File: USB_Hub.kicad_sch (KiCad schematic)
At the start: 20 parts, among them U6 USB2514B_Bi, X1 24MHz

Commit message: Better schematics structure & Hub sub-circuit connections
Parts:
- removed R6, R7, R8: 100k, Resistor_SMD:R_0603_1608Metric, symbol Device:R
- added C14: 100u, Capacitor_SMD:C_1206_3216Metric, symbol Device:C
- added R18, R19, R20: 100k, Resistor_SMD:R_0603_1608Metric, symbol Device:R
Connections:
- net CFGS0: now also R20.2; no longer R11.2
- net CFGS1: now also R11.2
- net GND: now also C14.2, R18.1, R19.1, R20.1
- net NREM0: now also R18.2
- net NREM1: now also R19.2
- net VBUS: now also C14.1; no longer R4.2
- net USB1_DN renamed USB_DOWN_1/USB1_DP
- net USB1_DP renamed USB_DOWN_1/USB1_DN
- net USB2_DN renamed USB_DOWN_1/USB2_DN
- net USB2_DP renamed USB_DOWN_1/USB2_DP
- net USB3_DN renamed USB_DOWN_2/USB1_DP
- net USB3_DP renamed USB_DOWN_2/USB1_DN
- net USB4_DN renamed USB_DOWN_2/USB2_DN
- net USB4_DP renamed USB_DOWN_2/USB2_DP
- net VHUB renamed +3V3
- net +3V3: now also R4.2
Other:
- sheet USB_A_Conn renamed USB_DOWN_1
- added sheet USB_DOWN_2 (USB_A_Conn.kicad_sch)
- sheet USB_DOWN_1 ports: added USB1_DN, USB1_DP, USB2_DN, USB2_DP; removed none
- note added: "All PORTS are removable TABLE 3-2/3"
- note added: "CFG_SEL = 0b00 => Self-powered TABLE 5-1"
- note removed: "CFG_SEL = 0b10 => Bus-powered TABLE 5-1"
- note removed: "PORTS 1-3 are non-removable TABLE 3-2/3"
- moved on the sheet: C3, C4, C5, C6, X1

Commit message: Changed MCU & Stared routing HDMI connectiors
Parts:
- removed R4, R5: 100k, Resistor_SMD:R_0603_1608Metric, symbol Device:R
- added R19: 10k, Resistor_SMD:R_0402_1005Metric, symbol Device:R
- C1: renamed from C3; AX (none) -> 27004; AX no. 27004 -> (none)
- C10: renamed from C12; AX (none) -> 27012; AX no. 27012 -> (none)
- C2: renamed from C5; AX (none) -> 27012; AX no. 27012 -> (none)
- C3: renamed from C4; AX (none) -> 27004; AX no. 27004 -> (none)
- C4: renamed from C6; AX (none) -> 27012; AX no. 27012 -> (none)
- C5: renamed from C7; AX (none) -> 27012; AX no. 27012 -> (none)
- C6: renamed from C8; AX (none) -> 27012; AX no. 27012 -> (none)
- C7: renamed from C9; AX (none) -> 27012; AX no. 27012 -> (none)
- C8: renamed from C10; AX (none) -> 27012; AX no. 27012 -> (none)
- C9: renamed from C11; AX (none) -> 27012; AX no. 27012 -> (none)
- R3: renamed from R20; AX (none) -> 141003; AX no. 141003 -> (none)
- R4: renamed from R9; footprint Resistor_SMD:R_0603_1608Metric -> Resistor_SMD:R_0402_1005Metric; AX (none) -> 201002; AX no. 141002 -> (none)
- R5: renamed from R10; AX (none) -> 141202; AX no. 141202 -> (none)
- R6: renamed from R19; AX (none) -> 141003; AX no. 141003 -> (none)
- R7: renamed from R18; AX (none) -> 141003; AX no. 141003 -> (none)
- R8: renamed from R11; AX (none) -> 141003; AX no. 141003 -> (none)
- U1: renamed from U6; Name USB2514BT/M2 -> (none)
- X1: Name TSX-3225 24.0000MF20G-AC3 -> (none); private KLC_S4.1 -> (none)
- renumbered C14 to C11
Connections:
- net +3V3: now also R19.1
- net VBUS_DET: no longer names the net of U1.27 (VBUS_DET)
- net VBUS_DET: now also R19.2
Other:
- note added: "Suggested by the data sheet TABLE 3-2"
- note removed: "100k 2:1 voltage divider suggested by the data sheet TABLE 3-2"

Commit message: Schematics done
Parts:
- removed C10, C5, C6, C7, C8, C9: 100n, Capacitor_SMD:C_0603_1608Metric, symbol Device:C
- added C32, C33, C34, C35, C36, C37: 1u, Capacitor_SMD:C_0402_1005Metric, symbol Device:C
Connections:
- net +3V3: now also C32.1, C33.1, C34.1, C35.1, C36.1, C37.1
- net GND: now also C32.2, C33.2, C34.2, C35.2, C36.2, C37.2
- net UP_DET: now reaches R19.2, U1.27 (VBUS_DET)
- net USB_HOST_DN renamed USB_UP_DN
- net USB_HOST_DP renamed USB_UP_DP
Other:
- note added: "24 MHz +/- 350 ppm Internal 1Mohm resistor Datasheet 7.1 C=2*(C_{L}-C_{stray})=10pF"
- note removed: "24 MHz +/- 350 ppm Internal 1Mohm resistor Datasheet 7.1 C_{Load}=2*(C_{Xtal}-C_{Stray})=10pF"
- moved on the sheet: C11, R19

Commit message: Fixed DRC & Adnotations
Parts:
- renumbered C34 to C10, C35 to C11, C36 to C12, C37 to C13, C11 to C14, C1 to C4, C2 to C5, C3 to C6, C4 to C7, C32 to C8, C33 to C9, R6 to R10, R7 to R11, R8 to R12, R19 to R13, R3 to R7, R4 to R8, R5 to R9, U1 to U4

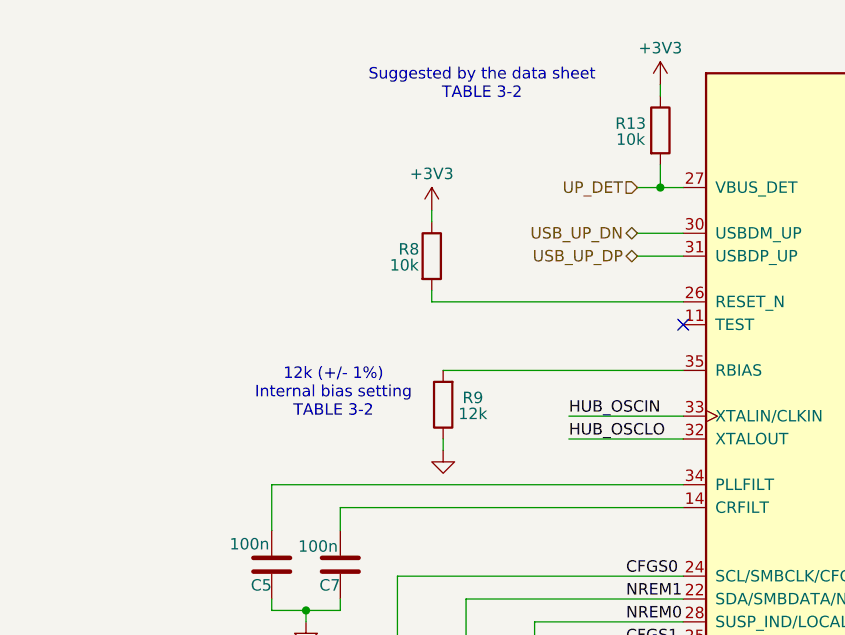
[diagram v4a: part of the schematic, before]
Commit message: Library and Schematics Fixes
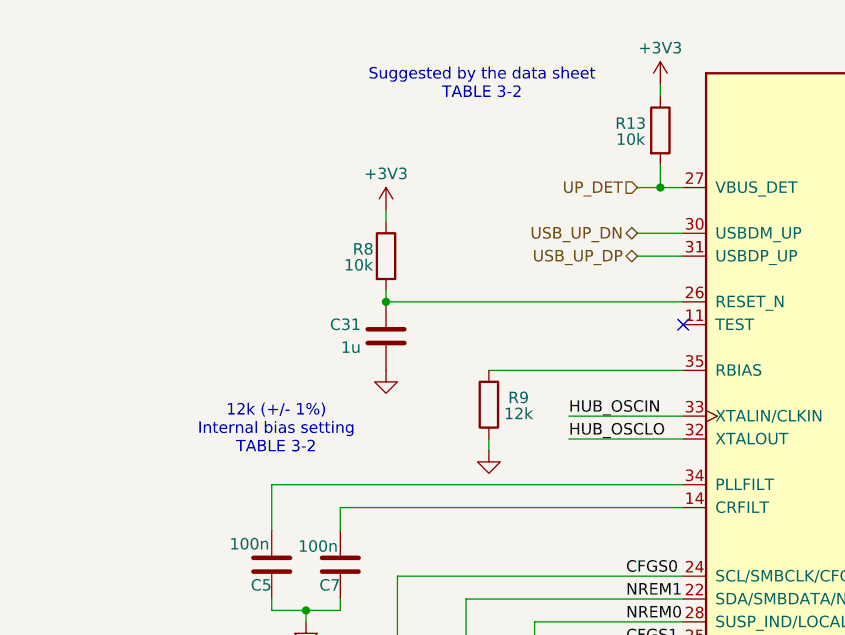
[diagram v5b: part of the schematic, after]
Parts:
- added C31: 1u, Capacitor_SMD:C_0402_1005Metric, symbol Device:C
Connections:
- net GND: now also C31.2
- net at R8.2, U4.26 (RESET_N): now also C31.1
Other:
- moved on the sheet: R8, R9
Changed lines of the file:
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@@
 	(text "12k (+/- 1%)\nInternal bias setting\nTABLE 3-2"
 		(exclude_from_sim no)
-		(at 88.138 119.38 0)
+		(at 81.788 123.444 0)
 		(effects
 			(font
@@
 	)
 	(junction
+		(at 93.98 109.22)
+		(diameter 0)
+		(color 0 0 0 0)
+	)
+	(junction
 		(at 106.68 158.75)
 		(diameter 0)
@@
 	(wire
 		(pts
-			(xy 100.33 125.73) (xy 100.33 124.46)
+			(xy 105.41 125.73) (xy 105.41 124.46)
 		)
 		(stroke
@@
 	(wire
 		(pts
-			(xy 99.06 109.22) (xy 127 109.22)
+			(xy 93.98 109.22) (xy 127 109.22)
 		)
 		(stroke
@@
 	(wire
 		(pts
-			(xy 99.06 107.95) (xy 99.06 109.22)
+			(xy 93.98 107.95) (xy 93.98 109.22)
 		)
 		(stroke
@@
 	(wire
 		(pts
-			(xy 99.06 99.06) (xy 99.06 100.33)
+			(xy 93.98 99.06) (xy 93.98 100.33)
 		)
 		(stroke
@@
 	(wire
 		(pts
-			(xy 100.33 116.84) (xy 127 116.84)
+			(xy 105.41 116.84) (xy 127 116.84)
 		)
 		(stroke
@@
 	(symbol
 		(lib_id "Device:R")
-		(at 100.33 120.65 180)
+		(at 105.41 120.65 180)
 		(unit 1)
 		(body_style 1)
@@
 		(dnp no)
 		(property "Reference" "R9"
-			(at 103.632 119.888 0)
+			(at 108.712 119.888 0)
 			(show_name no)
 			(do_not_autoplace no)
@@
 		)
 		(property "Value" "12k"
-			(at 103.632 121.666 0)
+			(at 108.712 121.666 0)
 			(show_name no)
 			(do_not_autoplace no)
@@
 		)
 		(property "Footprint" "Resistor_SMD:R_0603_1608Metric"
-			(at 102.108 120.65 90)
+			(at 107.188 120.65 90)
 			(hide yes)
 			(show_name no)
@@
 		)
 		(property "Datasheet" ""
-			(at 100.33 120.65 0)
+			(at 105.41 120.65 0)
 			(hide yes)
 			(show_name no)
@@
 		)
 		(property "Description" "Resistor"
-			(at 100.33 120.65 0)
+			(at 105.41 120.65 0)
 			(hide yes)
 			(show_name no)
@@
 		)
 		(property "AX" "141202"
-			(at 100.33 120.65 0)
+			(at 105.41 120.65 0)
 			(hide yes)
 			(show_name no)
@@
 	(symbol
 		(lib_id "power:+3V3")
-		(at 99.06 99.06 0)
+		(at 93.98 99.06 0)
 		(unit 1)
 		(body_style 1)
@@
 		(dnp no)
 		(property "Reference" "#PWR014"
-			(at 99.06 102.87 0)
+			(at 93.98 102.87 0)
 			(hide yes)
 			(show_name no)
@@
 		)
 		(property "Value" "+3V3"
-			(at 99.06 94.996 0)
+			(at 93.98 94.996 0)
 			(show_name no)
 			(do_not_autoplace no)
@@
 		)
 		(property "Footprint" ""
-			(at 99.06 99.06 0)
+			(at 93.98 99.06 0)
 			(hide yes)
 			(show_name no)
@@
 		)
 		(property "Datasheet" ""
-			(at 99.06 99.06 0)
+			(at 93.98 99.06 0)
 			(hide yes)
 			(show_name no)
@@
 		)
 		(property "Description" "Power symbol creates a global label with name \"+3V3\""
-			(at 99.06 99.06 0)
+			(at 93.98 99.06 0)
 			(hide yes)
 			(show_name no)
@@
 	(symbol
 		(lib_id "Device:C")
+		(at 93.98 113.03 0)
+		(mirror y)
+		(unit 1)
+		(body_style 1)
+		(exclude_from_sim no)
+		(in_bom yes)
+		(on_board yes)
+		(in_pos_files yes)
+		(dnp no)
+		(property "Reference" "C31"
+			(at 91.186 111.76 0)
+			(show_name no)
+			(do_not_autoplace no)
+			(effects
+				(font
+					(size 1.27 1.27)
+				)
+				(justify left)
+			)
+		)
+		(property "Value" "1u"
+			(at 91.186 114.3 0)
+			(show_name no)
+			(do_not_autoplace no)
+			(effects
+				(font
+					(size 1.27 1.27)
+				)
+				(justify left)
+			)
+		)
+		(property "Footprint" "Capacitor_SMD:C_0402_1005Metric"
+			(at 93.0148 116.84 0)
+			(hide yes)
+			(show_name no)
+			(do_not_autoplace no)
+			(effects
+				(font
+					(size 1.27 1.27)
+				)
+			)
+		)
+		(property "Datasheet" ""
+			(at 93.98 113.03 0)
+			(hide yes)
+			(show_name no)
+			(do_not_autoplace no)
+			(effects
+				(font
+					(size 1.27 1.27)
+				)
+			)
+		)
+		(property "Description" "Unpolarized capacitor"
+			(at 93.98 113.03 0)
+			(hide yes)
+			(show_name no)
+			(do_not_autoplace no)
+			(effects
+				(font
+					(size 1.27 1.27)
+				)
+			)
+		)
+		(property "AX" "27730"
+			(at 93.98 113.03 0)
+			(hide yes)
+			(show_name no)
+			(do_not_autoplace no)
+			(effects
+				(font
+					(size 1.27 1.27)
+				)
+			)
+		)
+		(pin "2"
+		)
+		(pin "1"
+		)
+		(instances
+			(project "KVM_Switch"
+				(path "/94386106-ccd4-487f-b5c5-d52ec3dd59db/0e1d684f-830c-4bab-be20-dfd6c92d7874"
+					(reference "C31")
+					(unit 1)
+				)
+			)
+		)
+	)
+	(symbol
+		(lib_id "Device:C")
 		(at 88.9 138.43 180)
 		(unit 1)
@@
 	)
 	(symbol
+		(lib_id "power:GND")
+		(at 93.98 116.84 0)
+		(unit 1)
+		(body_style 1)
+		(exclude_from_sim no)
+		(in_bom yes)
+		(on_board yes)
+		(in_pos_files yes)
+		(dnp no)
+		(fields_autoplaced yes)
+		(property "Reference" "#PWR038"
+			(at 93.98 123.19 0)
+			(hide yes)
+			(show_name no)
+			(do_not_autoplace no)
+			(effects
+				(font
+					(size 1.27 1.27)
+				)
+			)
+		)
+		(property "Value" "GND"
+			(at 93.98 121.92 0)
+			(hide yes)
+			(show_name no)
+			(do_not_autoplace no)
+			(effects
+				(font
+					(size 1.27 1.27)
+				)
+			)
+		)
+		(property "Footprint" ""
+			(at 93.98 116.84 0)
+			(hide yes)
+			(show_name no)
+			(do_not_autoplace no)
+			(effects
+				(font
+					(size 1.27 1.27)
+				)
+			)
+		)
+		(property "Datasheet" ""
+			(at 93.98 116.84 0)
+			(hide yes)
+			(show_name no)
+			(do_not_autoplace no)
+			(effects
+				(font
+					(size 1.27 1.27)
+				)
+			)
+		)
+		(property "Description" "Power symbol creates a global label with name \"GND\" , ground"
+			(at 93.98 116.84 0)
+			(hide yes)
+			(show_name no)
+			(do_not_autoplace no)
+			(effects
+				(font
+					(size 1.27 1.27)
+				)
+			)
+		)
+		(pin "1"
+		)
+		(instances
+			(project "KVM_Switch"
+				(path "/94386106-ccd4-487f-b5c5-d52ec3dd59db/0e1d684f-830c-4bab-be20-dfd6c92d7874"
+					(reference "#PWR038")
+					(unit 1)
+				)
+			)
+		)
+	)
+	(symbol
 		(lib_id "power:+3V3")
 		(at 124.46 85.09 0)
@@
 	(symbol
 		(lib_id "Device:R")
-		(at 99.06 104.14 0)
+		(at 93.98 104.14 0)
 		(unit 1)
 		(body_style 1)
@@
 		(dnp no)
 		(property "Reference" "R8"
-			(at 96.52 103.378 0)
+			(at 91.44 103.378 0)
 			(show_name no)
 			(do_not_autoplace no)
@@
 		)
 		(property "Value" "10k"
-			(at 96.012 105.156 0)
+			(at 90.932 105.156 0)
 			(show_name no)
 			(do_not_autoplace no)
@@
 		)
 		(property "Footprint" "Resistor_SMD:R_0402_1005Metric"
-			(at 97.282 104.14 90)
+			(at 92.202 104.14 90)
 			(hide yes)
 			(show_name no)
@@
 		)
 		(property "Datasheet" ""
-			(at 99.06 104.14 0)
+			(at 93.98 104.14 0)
 			(hide yes)
 			(show_name no)
@@
 		)
 		(property "Description" "Resistor"
-			(at 99.06 104.14 0)
+			(at 93.98 104.14 0)
 			(hide yes)
 			(show_name no)
@@
 		)
 		(property "AX" "201002"
-			(at 99.06 104.14 0)
+			(at 93.98 104.14 0)
 			(hide yes)
 			(show_name no)
@@
 	(symbol
 		(lib_id "power:GND")
-		(at 100.33 125.73 0)
+		(at 105.41 125.73 0)
 		(unit 1)
 		(body_style 1)
@@
 		(fields_autoplaced yes)
 		(property "Reference" "#PWR015"
-			(at 100.33 132.08 0)
+			(at 105.41 132.08 0)
 			(hide yes)
 			(show_name no)
@@
 		)
 		(property "Value" "GND"
-			(at 100.33 130.81 0)
+			(at 105.41 130.81 0)
 			(hide yes)
 			(show_name no)
@@
 		)
 		(property "Footprint" ""
-			(at 100.33 125.73 0)
+			(at 105.41 125.73 0)
 			(hide yes)
 			(show_name no)
@@
 		)
 		(property "Datasheet" ""
-			(at 100.33 125.73 0)
+			(at 105.41 125.73 0)
 			(hide yes)
 			(show_name no)
@@
 		)
 		(property "Description" "Power symbol creates a global label with name \"GND\" , ground"
-			(at 100.33 125.73 0)
+			(at 105.41 125.73 0)
 			(hide yes)
 			(show_name no)

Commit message: More schematics fixes & Layout attempt
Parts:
- C19: renamed from C4; footprint Capacitor_SMD:C_0603_1608Metric -> Capacitor_SMD:C_0402_1005Metric; AX 27004 -> 27705
- C20: renamed from C6; footprint Capacitor_SMD:C_0603_1608Metric -> Capacitor_SMD:C_0402_1005Metric; AX 27004 -> 27705
- C26: renamed from C5; footprint Capacitor_SMD:C_0603_1608Metric -> Capacitor_SMD:C_0402_1005Metric; AX 27012 -> 27726
- C27: renamed from C7; footprint Capacitor_SMD:C_0603_1608Metric -> Capacitor_SMD:C_0402_1005Metric; AX 27012 -> 27726
- R25: renamed from R7; footprint Resistor_SMD:R_0603_1608Metric -> Resistor_SMD:R_0402_1005Metric; AX 141003 -> 201003
- R26: renamed from R10; footprint Resistor_SMD:R_0603_1608Metric -> Resistor_SMD:R_0402_1005Metric; AX 141003 -> 201003
- R27: renamed from R11; footprint Resistor_SMD:R_0603_1608Metric -> Resistor_SMD:R_0402_1005Metric; AX 141003 -> 201003
- R28: renamed from R12; footprint Resistor_SMD:R_0603_1608Metric -> Resistor_SMD:R_0402_1005Metric; AX 141003 -> 201003
- renumbered C8 to C16, C9 to C17, C10 to C18, C11 to C21, C12 to C22, C13 to C23, C31 to C24, C14 to C25, R13 to R22, R8 to R23, R9 to R24, U4 to U13
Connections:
- net USB_DOWN_1/USB1_DN: now also U13.1 (USBDM_DN1/PRT_DIS_M1); no longer U13.2 (USBDP_DN1/PRT_DIS_P1)
- net USB_DOWN_1/USB1_DP: now also U13.2 (USBDP_DN1/PRT_DIS_P1); no longer U13.1 (USBDM_DN1/PRT_DIS_M1)
- net USB_DOWN_2/USB1_DN: now also U13.6 (USBDM_DN3/PRT_DIS_M3); no longer U13.7 (USBDP_DN3/PRT_DIS_P3)
- net USB_DOWN_2/USB1_DP: now also U13.7 (USBDP_DN3/PRT_DIS_P3); no longer U13.6 (USBDM_DN3/PRT_DIS_M3)
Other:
- company: (none) -> Stanisław Basiuk
- title: (none) -> KVM_Switch

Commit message: Added series resistors for USB_DET & SW, HubOsc testpoints
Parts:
- added TP17: TestPoint, TestPoint:TestPoint_Pad_D1.0mm, symbol Connector:TestPoint
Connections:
- net HUB_OSCIN: now also TP17.1
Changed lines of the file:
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@@
 	(text "24 MHz +/- 350 ppm\nInternal 1Mohm resistor\nDatasheet 7.1\nC=2*(C_{L}-C_{stray})=10pF"
 		(exclude_from_sim no)
-		(at 53.086 58.928 0)
+		(at 53.086 60.452 0)
 		(effects
 			(font
@@
 	)
 	(junction
+		(at 72.39 54.61)
+		(diameter 0)
+		(color 0 0 0 0)
+	)
+	(junction
 		(at 165.1 36.83)
 		(diameter 0)
@@
 	(wire
 		(pts
+			(xy 72.39 54.61) (xy 72.39 52.07)
+		)
+		(stroke
+			(width 0)
+			(type default)
+		)
+	)
+	(wire
+		(pts
 			(xy 127 147.32) (xy 118.11 147.32)
 		)
@@
 	(wire
 		(pts
-			(xy 72.39 55.88) (xy 72.39 52.07)
+			(xy 72.39 55.88) (xy 72.39 54.61)
 		)
 		(stroke
@@
 					(unit 1)
 				)
+			)
+		)
+	)
+	(symbol
+		(lib_id "Connector:TestPoint")
+		(at 72.39 54.61 90)
+		(unit 1)
+		(body_style 1)
+		(exclude_from_sim no)
+		(in_bom no)
+		(on_board yes)
+		(in_pos_files yes)
+		(dnp no)
+		(property "Reference" "TP17"
+			(at 65.786 54.61 90)
+			(show_name no)
+			(do_not_autoplace no)
+			(effects
+				(font
+					(size 1.27 1.27)
+				)
+			)
+		)
+		(property "Value" "TestPoint"
+			(at 69.088 52.07 90)
+			(hide yes)
+			(show_name no)
+			(do_not_autoplace no)
+			(effects
+				(font
+					(size 1.27 1.27)
+				)
+			)
+		)
+		(property "Footprint" "TestPoint:TestPoint_Pad_D1.0mm"
+			(at 72.39 49.53 0)
+			(hide yes)
+			(show_name no)
+			(do_not_autoplace no)
+			(effects
+				(font
+					(size 1.27 1.27)
+				)
+			)
+		)
+		(property "Datasheet" ""
+			(at 72.39 49.53 0)
+			(hide yes)
+			(show_name no)
+			(do_not_autoplace no)
+			(effects
+				(font
+					(size 1.27 1.27)
+				)
+			)
+		)
+		(property "Description" "test point"
+			(at 72.39 54.61 0)
+			(hide yes)
+			(show_name no)
+			(do_not_autoplace no)
+			(effects
+				(font
+					(size 1.27 1.27)
+				)
+			)
+		)
+		(pin "1"
+		)
+		(instances
+			(project "KVM_Switch"
+				(path "/94386106-ccd4-487f-b5c5-d52ec3dd59db/0e1d684f-830c-4bab-be20-dfd6c92d7874"
+					(reference "TP17")
+					(unit 1)
+				)
